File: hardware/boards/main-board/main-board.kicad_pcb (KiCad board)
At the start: 4 copper layers, 292.4 x 42 mm, 159 parts, among them J1 2x12 1.27mm shrouded box head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, J2 1x3, J4 12-way, J5 12-way, J6 8-way 2.54mm right-angle pin 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, Q1 AO3401A, SW1 KS-33, SW2 KS-33, SW3 KS-33, SW4 KS-33, SW5 KS-33, SW6 KS-33, SW7 KS-33, SW8 KS-33, U1 SP0504BAHT or equivalent 4-ch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, U10 MPXV4006DP, U11 SP0504BAHTG 4-channel 5V array, U2 MCP3202-CI/SN, U3 OPA2197IDR, U4 REF5050IDR, U5 R-78E5.0-1.0, U6 74AHCT125, U7 74HCS165, U8 74HCS165, U9 SP0504BAHTG 4-channel 5V array

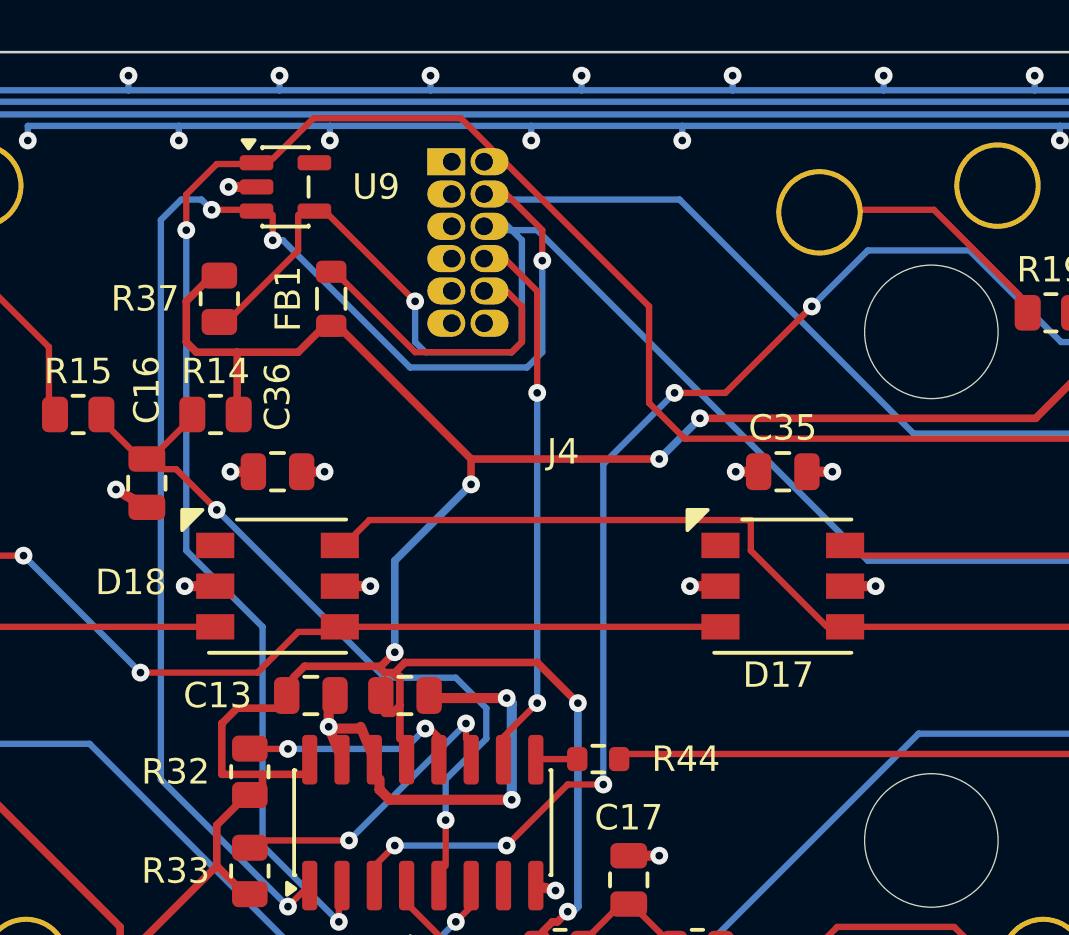
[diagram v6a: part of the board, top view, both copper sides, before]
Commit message: #35 pass 2: R12 (partly) — CHAIN_SHLD over the top of J4, one via fewer
U9.3 to J4.4 now runs on F over J4's top, outside SCK, and drops to B once
at x 135.1 to enter J4.4 from the east; the B U-loop under J4 and its vias
at 124.1,107.9 and 134.7,108.7 are gone (SHLD vias 10 -> 9). SER_LH's U-loop
stays: J4's even pins can only be entered from the east (the columns' pads
overlap and the rows are 0.2 mm apart), so every U9 line wraps J4, and the
only via-free wrap for SER would cross SCK's and SHLD's east exits. DRC 0/0;
pcb.py check 0 errors.

Gate-Red: known red, not this commit's: 37 deferred cad outputs, the module-iso coverage row (sim), module-main's kicad check; main-board renders/fab stale until the final render

Co-Authored-By: Claude Opus 5.5 <noreply@anthropic.com>
Claude-Session: https://claude.ai/code/session_01LmB4muFXnoLprWX4JzuJ5A
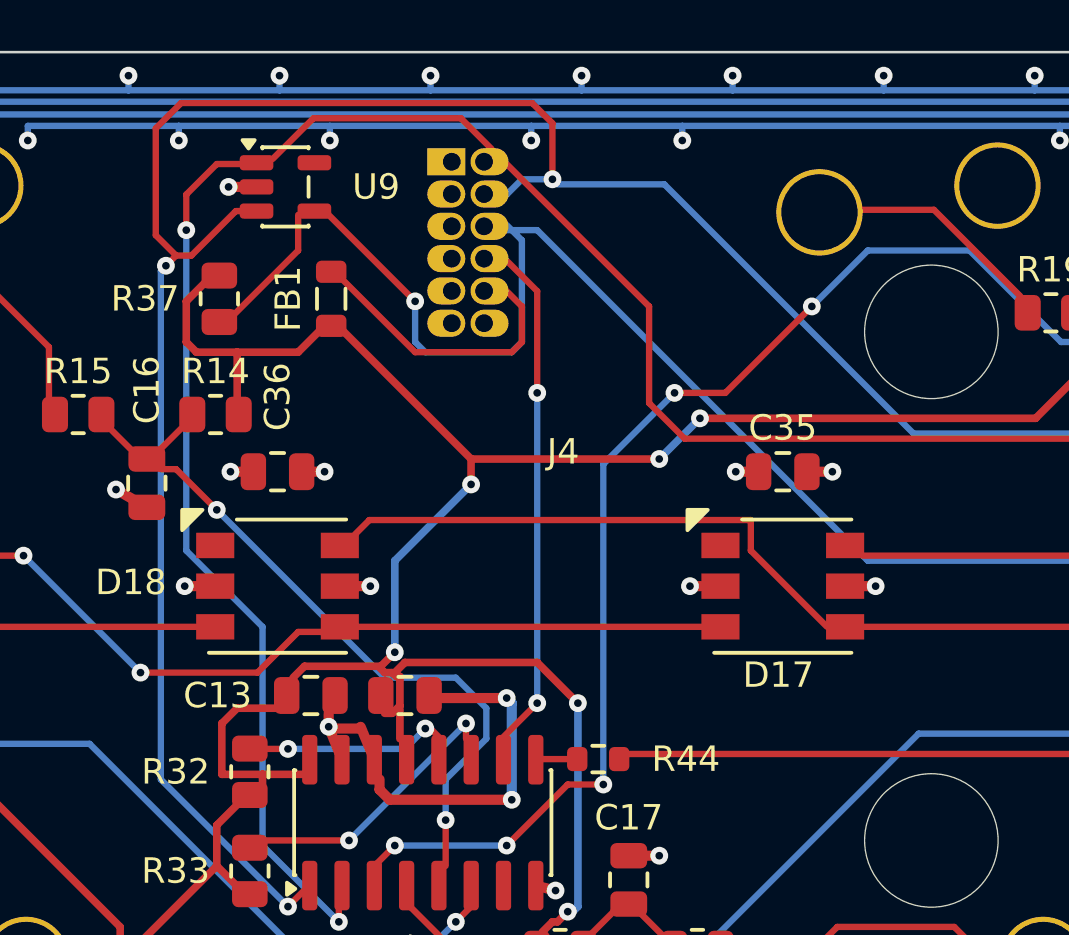
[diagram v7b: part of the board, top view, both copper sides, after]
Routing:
- net /CHAIN_SHLD: track 272.7 -> 276.1 mm, vias 10 -> 9
